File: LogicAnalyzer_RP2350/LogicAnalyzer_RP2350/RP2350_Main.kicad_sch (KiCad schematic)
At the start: 3 parts, among them U3 RP2350A

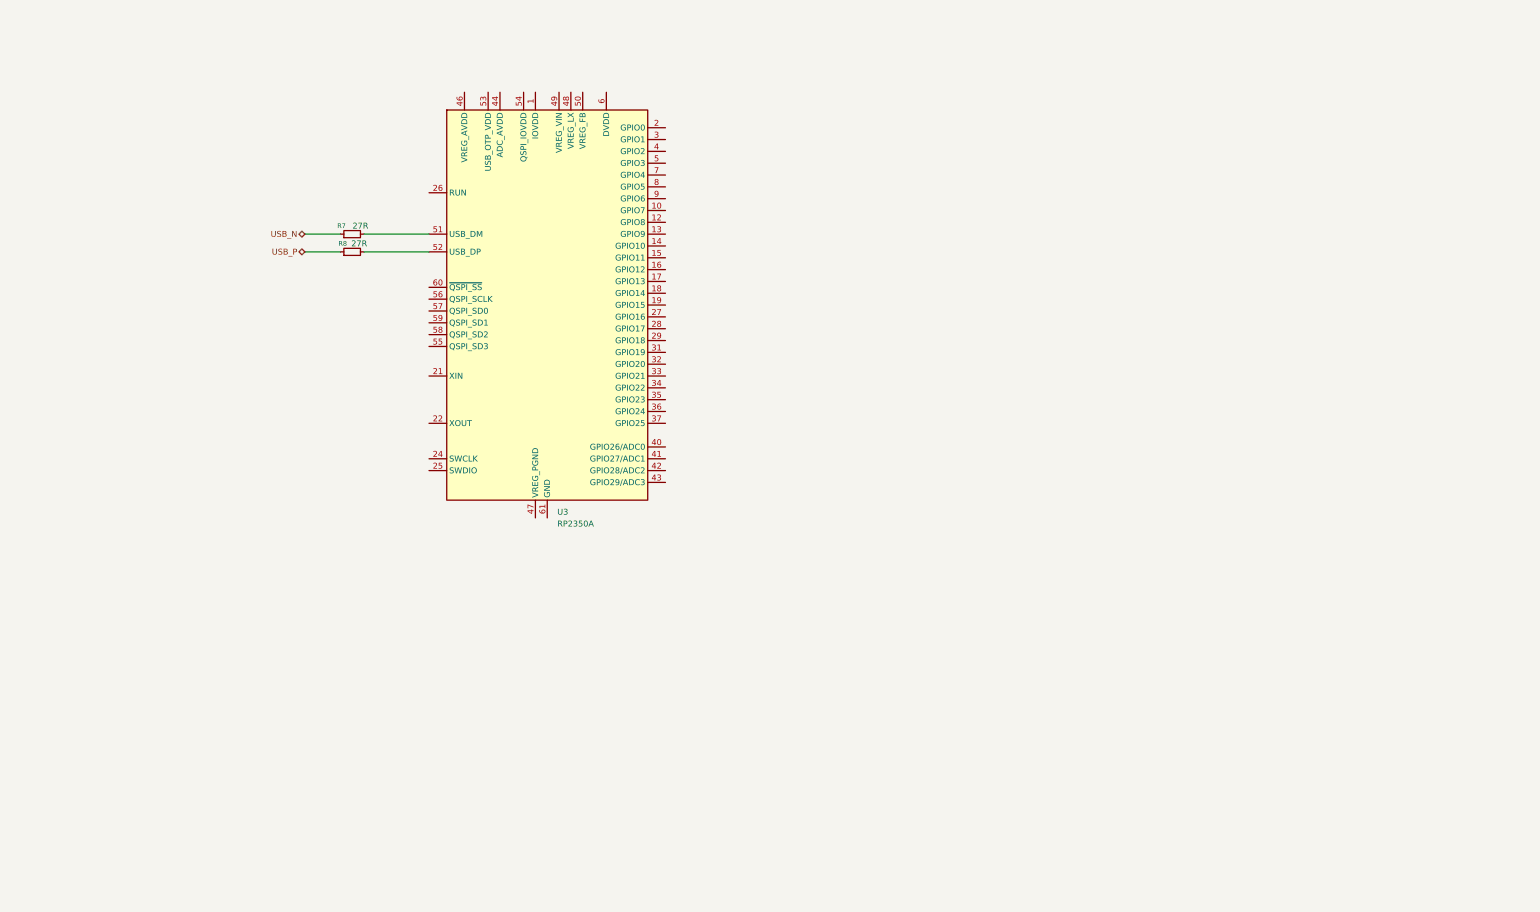
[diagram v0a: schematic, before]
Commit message: Completed VREG 1V1 and Decoupling the Power Pins
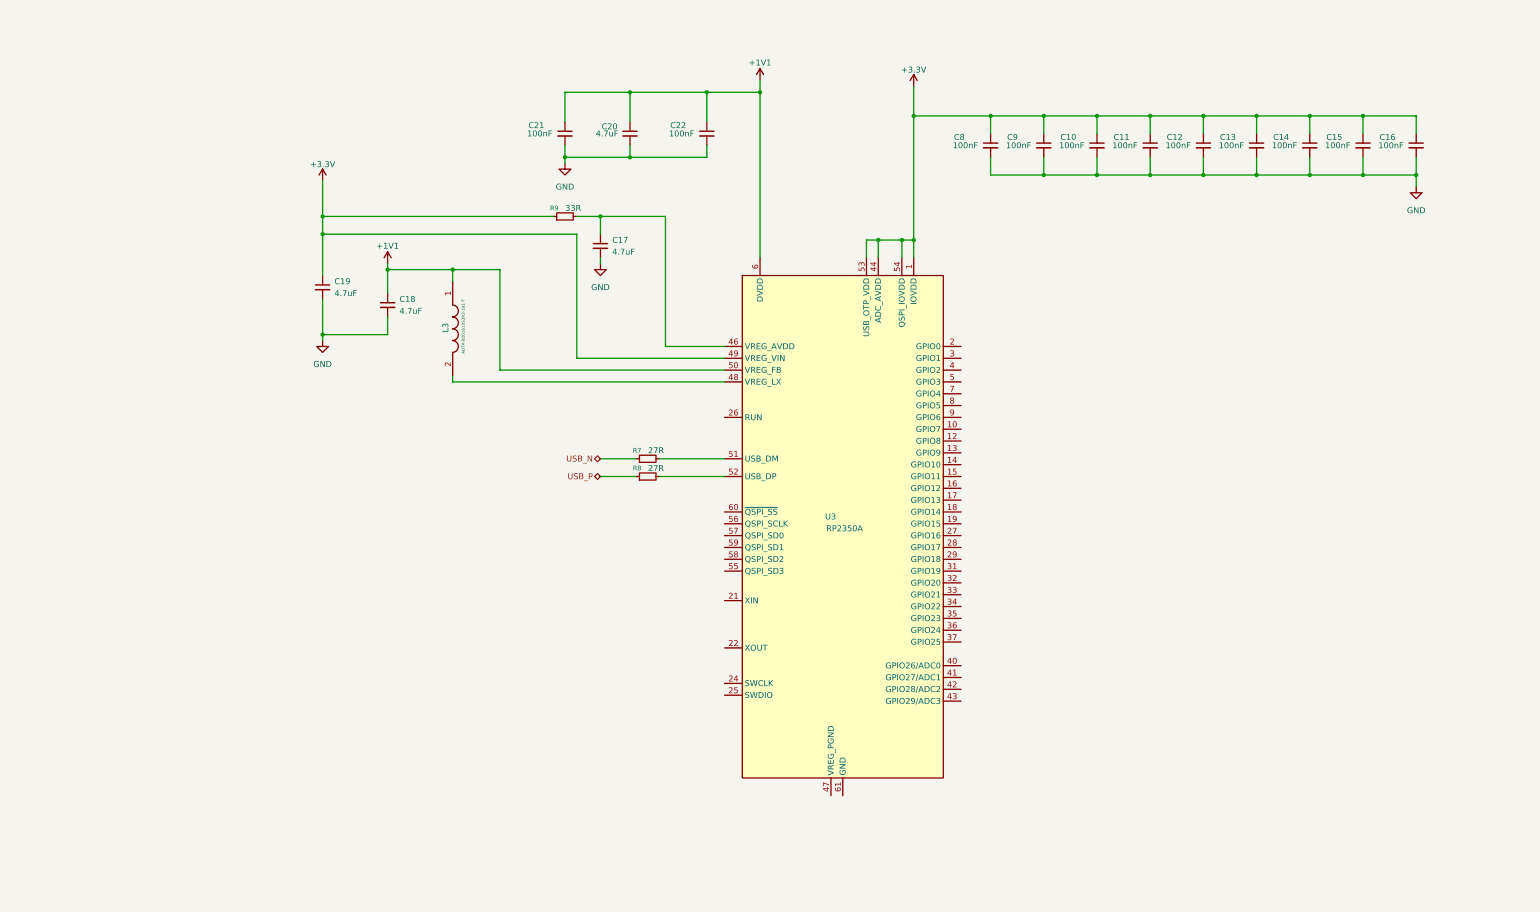
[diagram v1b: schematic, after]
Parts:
- added C10, C11, C12, C13, C14, C15, C16, C21, C22, C8, C9: 100nF, Capacitor_SMD:C_0603_1608Metric_Pad1.08x0.95mm_HandSolder, symbol Device:C_Small
- added C17, C18, C19, C20: 4.7uF, Capacitor_SMD:C_0603_1608Metric_Pad1.08x0.95mm_HandSolder, symbol Device:C_Small
- added L3: AOTA-B201610S3R3-101-T, AOTAB201610S3R3101T, symbol AOTA-B201610S3R3-101-T:AOTA-B201610S3R3-101-T
- added R9: 33R, Resistor_SMD:R_0603_1608Metric_Pad0.98x0.95mm_HandSolder, symbol Device:R_Small
- R7, R8: footprint Resistor_SMD:R_0402_1005Metric_Pad0.72x0.64mm_HandSolder -> Resistor_SMD:R_0603_1608Metric_Pad0.98x0.95mm_HandSolder
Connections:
- net +3.3V: now reaches U3.1 (IOVDD), U3.11 (IOVDD), U3.20 (IOVDD), U3.30 (IOVDD), U3.38 (IOVDD), U3.45 (IOVDD)
- net +3.3V: now also U3.44 (ADC_AVDD), U3.49 (VREG_VIN), U3.53 (USB_OTP_VDD), U3.54 (QSPI_IOVDD), C10.1, C11.1, C12.1, C13.1, C14.1, C15.1, C16.1, C19.1, C8.1, C9.1, R9.1
- net +1V1: now reaches U3.23 (DVDD), U3.39 (DVDD), U3.6 (DVDD)
- net +1V1: now also U3.50 (VREG_FB), C18.1, C20.1, C21.1, C22.1, L3.1
- net at U3.46 (VREG_AVDD): now also C17.1, R9.2
- net at U3.48 (VREG_LX): now also L3.2
- new net GND: C10.2, C11.2, C12.2, C13.2, C14.2, C15.2, C16.2, C17.2, C18.2, C19.2, C20.2, C21.2, C22.2, C8.2, C9.2
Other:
- moved on the sheet: R7, U3

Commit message: Addded Crystal
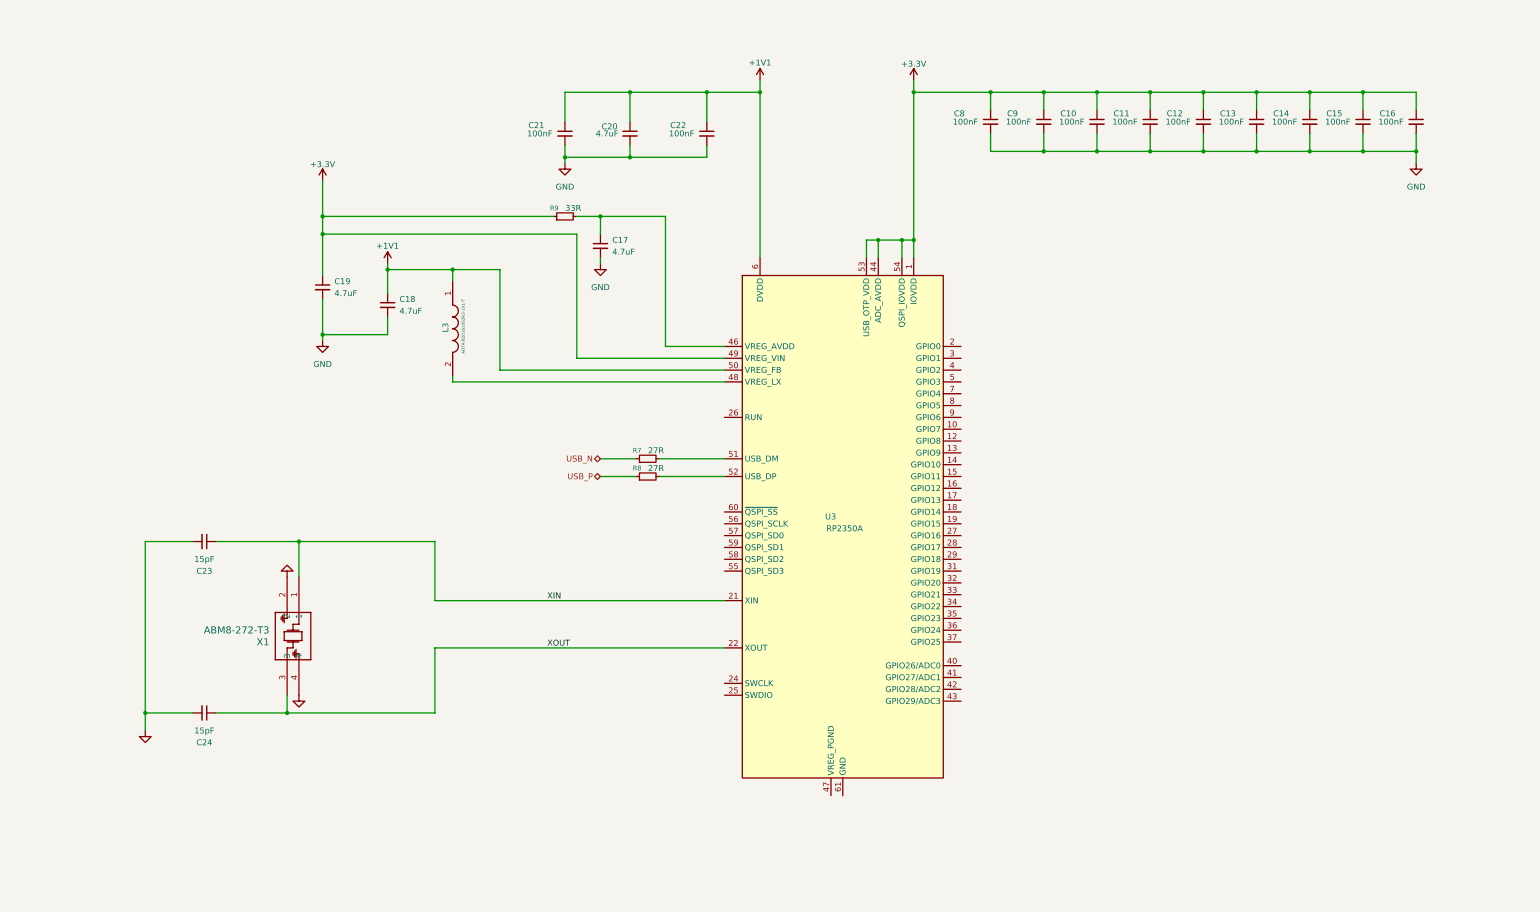
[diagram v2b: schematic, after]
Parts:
- added C23, C24: 15pF, Capacitor_SMD:C_0603_1608Metric_Pad1.08x0.95mm_HandSolder, symbol Device:C_Small
- added X1: ABM8-272-T3, ABM8-272-T3_ABR, symbol ABM8-272-T3:ABM8-272-T3
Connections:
- net GND: now also C23.2, C24.2, X1.2, X1.4
- net XIN: now reaches U3.21 (XIN)
- net XIN: now also C23.1, X1.1
- net XOUT: now reaches U3.22 (XOUT)
- net XOUT: now also C24.1, X1.3
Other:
- moved on the sheet: C10, C11, C12, C13, C14, C15, C16, C8, C9

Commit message: QSPIFLASH ADDED
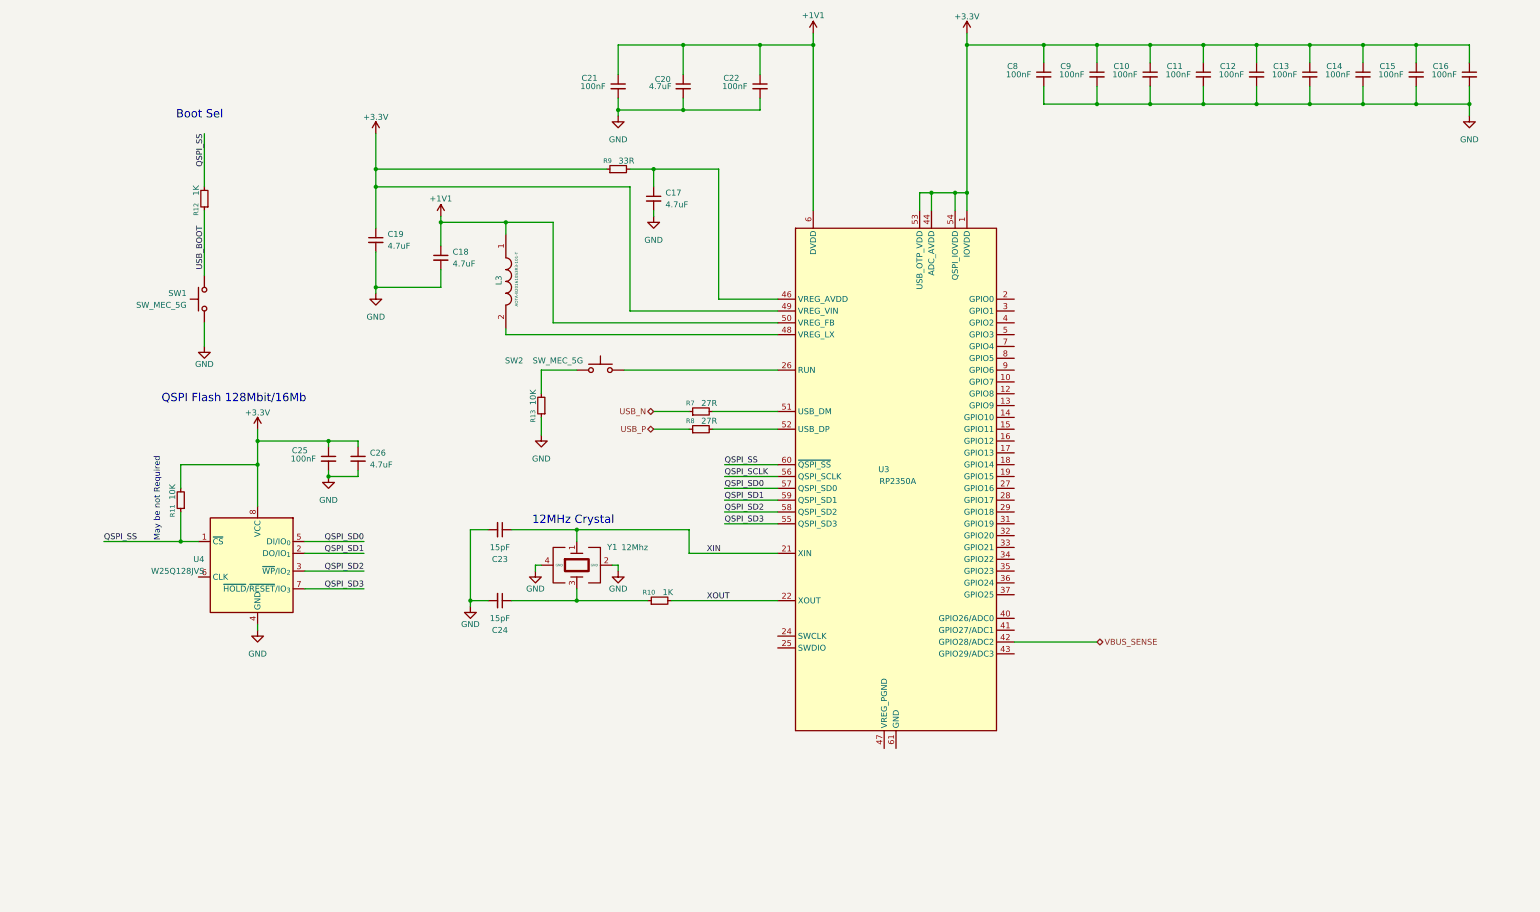
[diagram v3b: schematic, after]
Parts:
- removed X1: ABM8-272-T3, ABM8-272-T3_ABR, symbol ABM8-272-T3:ABM8-272-T3
- added C25: 100nF, Capacitor_SMD:C_0603_1608Metric_Pad1.08x0.95mm_HandSolder, symbol Device:C_Small
- added C26: 4.7uF, Capacitor_SMD:C_0603_1608Metric_Pad1.08x0.95mm_HandSolder, symbol Device:C_Small
- added R10, R12: 1K, Resistor_SMD:R_0603_1608Metric_Pad0.98x0.95mm_HandSolder, symbol Device:R_Small
- added R11, R13: 10K, Resistor_SMD:R_0603_1608Metric_Pad0.98x0.95mm_HandSolder, symbol Device:R_Small
- added SW1, SW2: SW_MEC_5G, SKRPABE010:SW4_SKRPABE010_ALPS, symbol Switch:SW_MEC_5G
- added U4: W25Q128JVS, Package_SO:SOIC-8_5.3x5.3mm_P1.27mm, symbol Memory_Flash:W25Q128JVS
- added Y1: 12Mhz, ABM8-272-T3:ABM8-272-T3_ABR, symbol Crystal-4Pins:Crystal_4Pins
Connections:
- net +3.3V: now also C25.1, C26.1, R11.2, U4.8 (VCC)
- net GND: now also C25.2, C26.2, R13.1, SW1.3 (B), SW1.4 (B), U4.4 (GND), Y1.2 (GND), Y1.4 (GND)
- net XIN: now also Y1.1
- net XOUT: now also R10.2; no longer C24.1
- net at U3.26 (RUN): now also SW2.1 (A), SW2.2 (A)
- net VBUS_SENSE: now reaches U3.42 (GPIO28/ADC2)
- net QSPI_SD3: now reaches U3.55 (QSPI_SD3)
- net QSPI_SD3: now also U4.7 (~{HOLD}/~{RESET}/IO_{3})
- net QSPI_SCLK: now reaches U3.56 (QSPI_SCLK)
- net QSPI_SD0: now reaches U3.57 (QSPI_SD0)
- net QSPI_SD0: now also U4.5 (DI/IO_{0})
- net QSPI_SD2: now reaches U3.58 (QSPI_SD2)
- net QSPI_SD2: now also U4.3 (~{WP}/IO_{2})
- net QSPI_SD1: now reaches U3.59 (QSPI_SD1)
- net QSPI_SD1: now also U4.2 (DO/IO_{1})
- net QSPI_SS: now reaches U3.60 (~{QSPI_SS})
- net QSPI_SS: now also R11.1, R12.2, U4.1 (~{CS})
- new net: C24.1, R10.1, Y1.3
- new net: R13.2, SW2.3 (B), SW2.4 (B)
- new net USB_BOOT: R12.1, SW1.1 (A), SW1.2 (A)
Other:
- note added: "12MHz Crystal"
- note added: "Boot Sel"
- note added: "May be not Required"
- note added: "QSPI Flash 128Mbit/16Mb"
- moved on the sheet: C10, C11, C12, C13, C14, C15, C16, C17, C18, C19, C20, C21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

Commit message: added Debug Probe and Debug LED
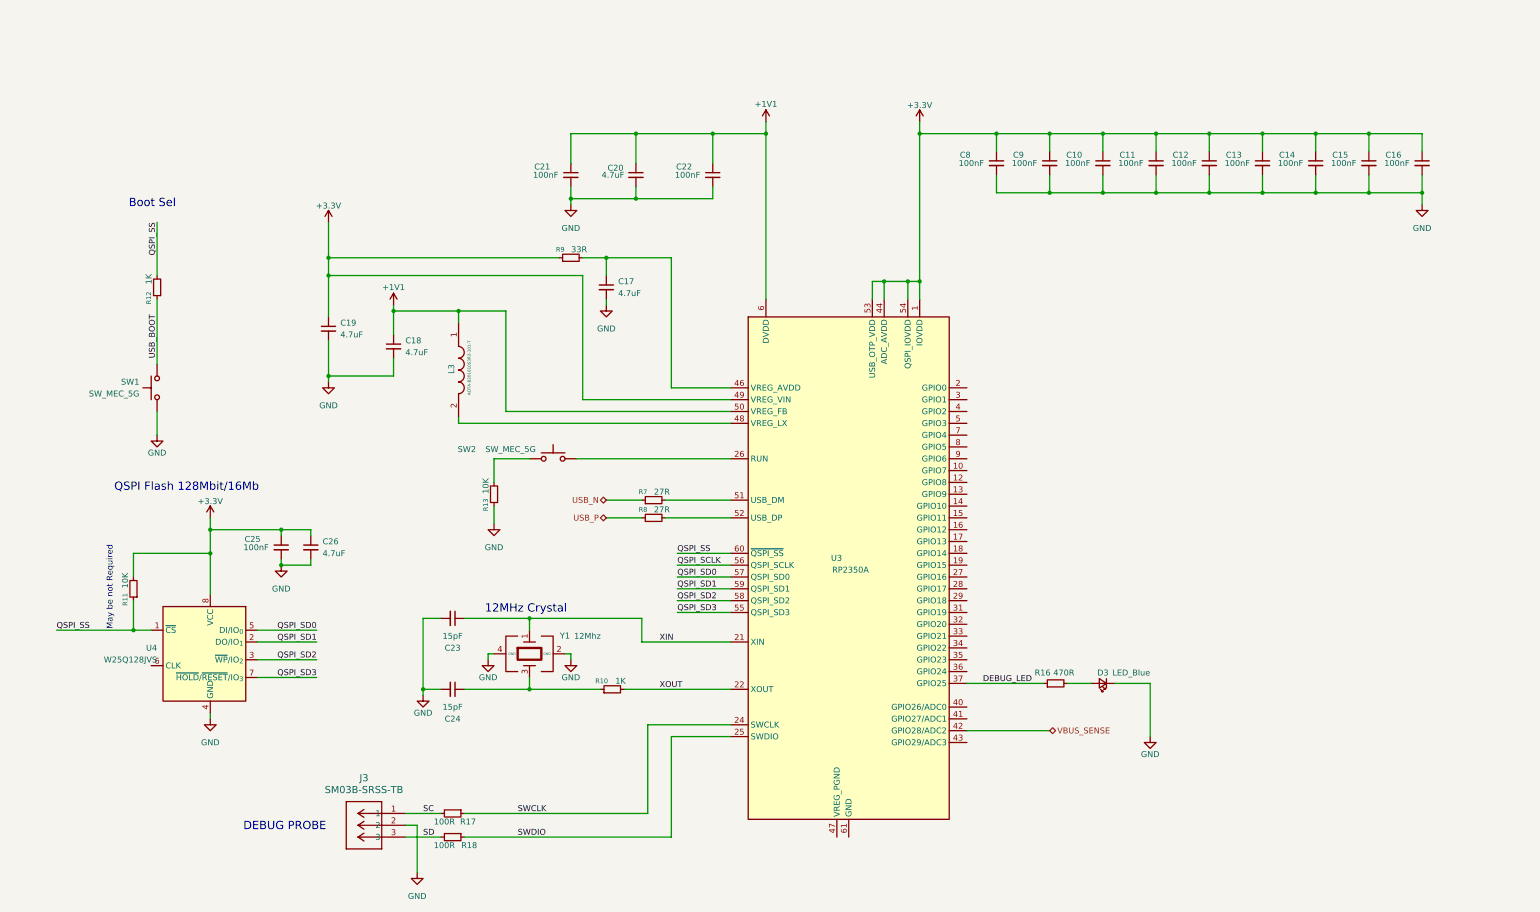
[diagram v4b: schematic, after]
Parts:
- added D3: LED_Blue, LED_SMD:LED_0603_1608Metric_Pad1.05x0.95mm_HandSolder, symbol Device:LED_Small
- added J3: SM03B-SRSS-TB, CONN_SM03B-SRSS-TB_JST, symbol SM03B-SRSS-TB:SM03B-SRSS-TB
- added R16: 470R, Resistor_SMD:R_0603_1608Metric_Pad0.98x0.95mm_HandSolder, symbol Device:R_Small
- added R17, R18: 100R, Resistor_SMD:R_0603_1608Metric_Pad0.98x0.95mm_HandSolder, symbol Device:R_Small
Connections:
- net GND: now also D3.1 (K), J3.2
- net SWCLK: now reaches U3.24 (SWCLK)
- net SWCLK: now also R17.1
- net SWDIO: now reaches U3.25 (SWDIO)
- net SWDIO: now also R18.1
- net DEBUG_LED: now reaches U3.37 (GPIO25)
- net DEBUG_LED: now also R16.1
- new net: D3.2 (A), R16.2
- new net SC: J3.1, R17.2
- new net SD: J3.3, R18.2
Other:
- note added: "DEBUG PROBE"
- moved on the sheet: C10, C11, C12, C13, C14, C15, C16, C17, C18, C19, C20, C21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
